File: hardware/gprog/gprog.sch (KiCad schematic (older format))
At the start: 23 parts, among them IC1 ATMEGA48P, P1 ISP x2560, P2 USB, P3 ISP x48, U1 74HC126, X1 12MHz

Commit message: gPROG: Dare I say the last, final draft.
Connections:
- net at U1.1, U1.13 (~E): now also JP1.2, R8.1, U1.10 (~E), U1.4 (~E)
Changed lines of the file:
@@
-EESchema Schematic File Version 2  date 27/11/2011 12:21:00 p.m.
+EESchema Schematic File Version 2  date 27/11/2011 8:31:10 p.m.
 LIBS:power
 LIBS:device
@@
 Sheet 1 1
 Title "G9X USB Programmer"
-Date "26 nov 2011"
+Date "27 nov 2011"
 Rev "1.0"
 Comp ""
@@
 Comment4 ""
 $EndDescr
+Connection ~ 7150 2400
+Wire Wire Line
+	8050 2400 7100 2400
+Connection ~ 8850 5150
+Wire Wire Line
+	8850 4750 8850 5150
+Wire Wire Line
+	6250 3200 6000 3200
+Wire Wire Line
+	6000 3200 6000 3450
+Wire Wire Line
+	7150 2400 7150 3950
+Wire Wire Line
+	7150 3950 8000 3950
+Wire Wire Line
+	8000 3950 8000 4000
+Connection ~ 1750 3550
+Wire Wire Line
+	1750 4350 1750 4100
+Wire Wire Line
+	1350 4100 1350 4250
+Wire Wire Line
+	1350 4250 2150 4250
+Wire Wire Line
+	2150 4250 2150 4100
+Connection ~ 2750 6950
+Wire Wire Line
+	2750 7050 2750 6950
+Connection ~ 3100 6350
+Wire Wire Line
+	3100 6500 3100 6350
+Wire Wire Line
+	2450 6350 2350 6350
+Wire Wire Line
+	3200 6350 3050 6350
+Connection ~ 2550 5850
+Wire Wire Line
+	2550 5750 2550 5850
+Wire Wire Line
+	3200 5150 2900 5150
+Wire Wire Line
+	3200 5350 2900 5350
+Wire Wire Line
+	3200 5550 2900 5550
+Wire Wire Line
+	5150 5550 5450 5550
+Connection ~ 4200 6850
+Wire Wire Line
+	4300 6850 4100 6850
+Wire Wire Line
+	4200 3950 4200 4100
+Wire Wire Line
+	9600 5550 9300 5550
+Wire Wire Line
+	9600 5350 9000 5350
+Wire Wire Line
+	9600 5150 8600 5150
+Wire Wire Line
+	7600 1950 6750 1950
+Wire Wire Line
+	7250 3600 6750 3600
+Wire Wire Line
+	9600 3150 9450 3150
+Wire Wire Line
+	9450 3150 9450 3550
+Wire Wire Line
+	9600 3050 8400 3050
+Wire Wire Line
+	8400 3050 8400 3600
+Wire Wire Line
+	8400 3600 8150 3600
+Connection ~ 8050 2400
+Wire Wire Line
+	9600 2650 9150 2650
+Wire Wire Line
+	9150 2650 9150 1950
+Wire Wire Line
+	9150 1950 8500 1950
+Wire Wire Line
+	2500 2600 2500 2250
+Wire Wire Line
+	2500 2600 2550 2600
+Wire Wire Line
+	4150 1950 4150 1700
+Wire Wire Line
+	5000 1800 5300 1800
+Wire Wire Line
+	3250 3150 3250 3050
+Connection ~ 3600 2600
+Wire Wire Line
+	3600 2650 3600 2600
+Wire Wire Line
+	3250 2600 3250 2650
+Wire Wire Line
+	3050 2600 4500 2600
+Wire Wire Line
+	3800 2350 3800 2400
+Connection ~ 4150 1800
+Wire Wire Line
+	2500 2250 1950 2250
+Wire Wire Line
+	2200 1800 2200 2050
+Wire Wire Line
+	2200 2050 1950 2050
+Wire Wire Line
+	1950 2350 2200 2350
+Wire Wire Line
+	2200 2350 2200 2650
+Wire Wire Line
+	2500 2150 2500 1800
+Wire Wire Line
+	2500 2150 1950 2150
+Wire Wire Line
+	3800 1950 3800 1800
+Connection ~ 3800 1800
+Wire Wire Line
+	4150 2400 4150 2350
+Connection ~ 3250 2600
+Wire Wire Line
+	3600 3050 3600 3150
+Wire Wire Line
+	5000 2600 5300 2600
+Wire Wire Line
+	4150 1200 4150 1150
+Wire Wire Line
+	4500 1800 3100 1800
+Wire Wire Line
+	2500 1800 2600 1800
+Wire Wire Line
+	9600 2850 8500 2850
+Wire Wire Line
+	9600 2750 8800 2750
+Wire Wire Line
+	8800 2750 8800 2400
+Wire Wire Line
+	8050 2250 8050 2550
+Wire Wire Line
+	8450 4300 8800 4300
+Wire Wire Line
+	8800 4300 8800 2950
+Wire Wire Line
+	8800 2950 9600 2950
+Wire Wire Line
+	7550 4300 6750 4300
+Wire Wire Line
+	7600 2850 6750 2850
+Wire Wire Line
+	9600 5050 9000 5050
+Wire Wire Line
+	9600 5250 9000 5250
+Wire Wire Line
+	9600 5450 9000 5450
+Wire Wire Line
+	9300 5550 9300 5800
+Wire Wire Line
+	4300 4100 4100 4100
+Connection ~ 4200 4100
+Wire Wire Line
+	4200 7000 4200 6850
+Wire Wire Line
+	3200 5650 2900 5650
+Wire Wire Line
+	3200 5450 2900 5450
+Wire Wire Line
+	3200 5250 2900 5250
+Wire Wire Line
+	2100 5850 3200 5850
+Wire Wire Line
+	2550 5150 2550 5250
+Wire Wire Line
+	3200 6150 2350 6150
+Wire Wire Line
+	2350 6150 2350 6500
+Connection ~ 2350 6350
+Wire Wire Line
+	3100 6900 3100 6950
+Wire Wire Line
+	3100 6950 2350 6950
+Wire Wire Line
+	2350 6950 2350 6900
+Wire Wire Line
+	6500 2150 6500 2400
+Wire Wire Line
+	6500 2400 6600 2400
+Connection ~ 1750 4250
+Wire Wire Line
+	1350 3700 1350 3550
+Wire Wire Line
+	1350 3550 2150 3550
+Wire Wire Line
+	2150 3550 2150 3700
+Wire Wire Line
+	1750 3450 1750 3700
+Wire Wire Line
+	7700 3300 7700 3200
+Connection ~ 7150 3200
+Wire Wire Line
+	7700 3200 6850 3200
+Wire Wire Line
+	8600 5150 8600 4750
 $Comp
 L +5V #PWR01
@@
 	1    0    0    -1
 $EndComp
-Wire Wire Line
-	8600 5150 8600 4750
-Wire Wire Line
-	6850 3200 7700 3200
-Connection ~ 7150 3200
-Wire Wire Line
-	7700 3200 7700 3300
-Wire Wire Line
-	1750 3450 1750 3700
-Wire Wire Line
-	2150 3550 2150 3700
-Wire Wire Line
-	2150 3550 1350 3550
-Wire Wire Line
-	1350 3550 1350 3700
-Connection ~ 1750 4250
-Wire Wire Line
-	6600 2400 6500 2400
-Wire Wire Line
-	6500 2400 6500 2150
-Wire Wire Line
-	2350 6950 2350 6900
-Wire Wire Line
-	2350 6950 3100 6950
-Wire Wire Line
-	3100 6950 3100 6900
-Connection ~ 2350 6350
-Wire Wire Line
-	2350 6500 2350 6150
-Wire Wire Line
-	2350 6150 3200 6150
-Wire Wire Line
-	2550 5150 2550 5250
-Wire Wire Line
-	2100 5850 3200 5850
-Wire Wire Line
-	3200 5250 2900 5250
-Wire Wire Line
-	3200 5450 2900 5450
-Wire Wire Line
-	3200 5650 2900 5650
-Wire Wire Line
-	4200 7000 4200 6850
-Connection ~ 4200 4100
-Wire Wire Line
-	4300 4100 4100 4100
-Wire Wire Line
-	9300 5800 9300 5550
-Wire Wire Line
-	9600 5450 9000 5450
-Wire Wire Line
-	9600 5250 9000 5250
-Wire Wire Line
-	9600 5050 9000 5050
-Wire Wire Line
-	7600 2850 6750 2850
-Wire Wire Line
-	7550 4300 6750 4300
-Wire Wire Line
-	9600 2950 8800 2950
-Wire Wire Line
-	8800 2950 8800 4300
-Wire Wire Line
-	8800 4300 8450 4300
-Wire Wire Line
-	8050 2250 8050 2550
-Wire Wire Line
-	8800 2400 8800 2750
-Wire Wire Line
-	8800 2750 9600 2750
-Wire Wire Line
-	9600 2850 8500 2850
-Wire Wire Line
-	2600 1800 2500 1800
-Wire Wire Line
-	4500 1800 3100 1800
-Wire Wire Line
-	4150 1200 4150 1150
-Wire Wire Line
-	5000 2600 5300 2600
-Wire Wire Line
-	3600 3050 3600 3150
-Connection ~ 3250 2600
-Wire Wire Line
-	4150 2400 4150 2350
-Connection ~ 3800 1800
-Wire Wire Line
-	3800 1950 3800 1800
-Wire Wire Line
-	1950 2150 2500 2150
-Wire Wire Line
-	2500 2150 2500 1800
-Wire Wire Line
-	2200 2650 2200 2350
-Wire Wire Line
-	2200 2350 1950 2350
-Wire Wire Line
-	1950 2050 2200 2050
-Wire Wire Line
-	2200 2050 2200 1800
-Wire Wire Line
-	1950 2250 2500 2250
-Connection ~ 4150 1800
-Wire Wire Line
-	3800 2350 3800 2400
-Wire Wire Line
-	3050 2600 4500 2600
-Wire Wire Line
-	3250 2600 3250 2650
-Wire Wire Line
-	3600 2650 3600 2600
-Connection ~ 3600 2600
-Wire Wire Line
-	3250 3150 3250 3050
-Wire Wire Line
-	5000 1800 5300 1800
-Wire Wire Line
-	4150 1950 4150 1700
-Wire Wire Line
-	2550 2600 2500 2600
-Wire Wire Line
-	2500 2600 2500 2250
-Wire Wire Line
-	8500 1950 9150 1950
-Wire Wire Line
-	9150 1950 9150 2650
-Wire Wire Line
-	9150 2650 9600 2650
-Connection ~ 8050 2400
-Wire Wire Line
-	8150 3600 8400 3600
-Wire Wire Line
-	8400 3600 8400 3050
-Wire Wire Line
-	8400 3050 9600 3050
-Wire Wire Line
-	9450 3550 9450 3150
-Wire Wire Line
-	9450 3150 9600 3150
-Wire Wire Line
-	7250 3600 6750 3600
-Wire Wire Line
-	7600 1950 6750 1950
-Wire Wire Line
-	9600 5150 8600 5150
-Wire Wire Line
-	9600 5350 9000 5350
-Wire Wire Line
-	9300 5550 9600 5550
-Wire Wire Line
-	4200 3950 4200 4100
-Wire Wire Line
-	4300 6850 4100 6850
-Connection ~ 4200 6850
-Wire Wire Line
-	5150 5550 5450 5550
-Wire Wire Line
-	3200 5550 2900 5550
-Wire Wire Line
-	3200 5350 2900 5350
-Wire Wire Line
-	3200 5150 2900 5150
-Wire Wire Line
-	2550 5750 2550 5850
-Connection ~ 2550 5850
-Wire Wire Line
-	3200 6350 3050 6350
-Wire Wire Line
-	2450 6350 2350 6350
-Wire Wire Line
-	3100 6500 3100 6350
-Connection ~ 3100 6350
-Wire Wire Line
-	2750 7050 2750 6950
-Connection ~ 2750 6950
-Wire Wire Line
-	2150 4250 2150 4100
-Wire Wire Line
-	2150 4250 1350 4250
-Wire Wire Line
-	1350 4250 1350 4100
-Wire Wire Line
-	1750 4350 1750 4100
-Connection ~ 1750 3550
-Wire Wire Line
-	8000 4000 8000 3950
-Wire Wire Line
-	7150 3950 8000 3950
-Wire Wire Line
-	7150 2400 7150 3950
-Connection ~ 7150 2400
-Wire Wire Line
-	6000 3450 6000 3200
-Wire Wire Line
-	6000 3200 6250 3200
-Wire Wire Line
-	8850 4750 8850 5150
-Connection ~ 8850 5150
 $Comp
 L VCC #PWR02

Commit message: Major changes to gprog, after prototype revealed multiple problems. Also reverted to TQFP-32 package instead of QFN/MLF.
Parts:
- removed JP1: ENABLE, symbol JUMPER
- added D5, D6: LED, symbol LED
- added D7: DIODESCH, symbol DIODESCH
- added R4, R9: 1K, symbol R
- U1: value 74HC126 -> 74HC125; symbol 74LS126 -> 74LS125
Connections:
- net labels added: BUF_ENABLE
- wire segments 92 -> 101
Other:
- note added: "Target Vcc is \n74HC125 only"
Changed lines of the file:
@@
-EESchema Schematic File Version 2  date 27/11/2011 8:31:10 p.m.
+EESchema Schematic File Version 2  date 13/12/2011 4:09:18 p.m.
 LIBS:power
 LIBS:device
@@
 Sheet 1 1
 Title "G9X USB Programmer"
-Date "27 nov 2011"
-Rev "1.0"
+Date "13 dec 2011"
+Rev "0.2"
 Comp ""
 Comment1 "Customised for G9X by JWB. Converted ro KiCAD by Gruvin"
@@
 Comment4 ""
 $EndDescr
+$Comp
+L VCC #PWR?
+U 1 1 4EE6C1C8
+P 8800 2400
+F 0 "#PWR?" H 8800 2500 30  0001 C CNN
+F 1 "VCC" H 8800 2500 30  0000 C CNN
+	1    8800 2400
+	1    0    0    -1
+$EndComp
+Text Notes 7300 5350 0    60   ~ 0
+Target Vcc is \n74HC125 only
+Wire Wire Line
+	8000 5150 7750 5150
+Connection ~ 5500 3150
+Wire Wire Line
+	5500 3050 5500 3150
+Wire Wire Line
+	5700 3750 5700 3850
+Wire Wire Line
+	5700 4250 5700 4650
+Wire Wire Line
+	5700 4650 5150 4650
+Wire Wire Line
+	5150 4850 5800 4850
 Connection ~ 7150 2400
 Wire Wire Line
-	8050 2400 7100 2400
-Connection ~ 8850 5150
-Wire Wire Line
-	8850 4750 8850 5150
-Wire Wire Line
-	6250 3200 6000 3200
-Wire Wire Line
-	6000 3200 6000 3450
+	7100 2400 8050 2400
 Wire Wire Line
 	7150 2400 7150 3950
@@
 	9600 5350 9000 5350
 Wire Wire Line
-	9600 5150 8600 5150
-Wire Wire Line
 	7600 1950 6750 1950
 Wire Wire Line
@@
 Connection ~ 3600 2600
 Wire Wire Line
-	3600 2650 3600 2600
-Wire Wire Line
-	3250 2600 3250 2650
+	3600 2600 3600 2650
+Wire Wire Line
+	3250 2650 3250 2600
 Wire Wire Line
 	3050 2600 4500 2600
@@
 	2500 2150 1950 2150
 Wire Wire Line
-	3800 1950 3800 1800
+	3800 1800 3800 1950
 Connection ~ 3800 1800
 Wire Wire Line
@@
 Connection ~ 7150 3200
 Wire Wire Line
-	7700 3200 6850 3200
+	7700 3200 6450 3200
 Wire Wire Line
 	8600 5150 8600 4750
+Wire Wire Line
+	5150 4550 5300 4550
+Wire Wire Line
+	5300 4550 5300 4250
+Wire Wire Line
+	5300 3850 5300 3750
+Wire Wire Line
+	5300 3250 5300 3150
+Wire Wire Line
+	5300 3150 5700 3150
+Wire Wire Line
+	5700 3150 5700 3250
+Wire Wire Line
+	8400 5150 9600 5150
+Connection ~ 8600 5150
+$Comp
+L DIODESCH D7
+U 1 1 4EE6C02E
+P 8200 5150
+F 0 "D7" H 8200 5250 40  0000 C CNN
+F 1 "DIODESCH" H 8200 5050 40  0000 C CNN
+	1    8200 5150
+	-1   0    0    1
+$EndComp
 $Comp
 L +5V #PWR01
-U 1 1 4ED164AA
-P 8800 2400
-F 0 "#PWR01" H 8800 2490 20  0001 C CNN
-F 1 "+5V" H 8800 2490 30  0000 C CNN
-	1    8800 2400
-	1    0    0    -1
-$EndComp
-$Comp
-L VCC #PWR02
+U 1 1 4EE6B3E0
+P 5500 3050
+F 0 "#PWR01" H 5500 3140 20  0001 C CNN
+F 1 "+5V" H 5500 3140 30  0000 C CNN
+	1    5500 3050
+	1    0    0    -1
+$EndComp
+$Comp
+L R R9
+U 1 1 4EE6B3BF
+P 5700 3500
+F 0 "R9" V 5780 3500 50  0000 C CNN
+F 1 "1K" V 5700 3500 50  0000 C CNN
+	1    5700 3500
+	-1   0    0    1
+$EndComp
+$Comp
+L R R4
+U 1 1 4EE6B3B8
+P 5300 3500
+F 0 "R4" V 5380 3500 50  0000 C CNN
+F 1 "1K" V 5300 3500 50  0000 C CNN
+	1    5300 3500
+	-1   0    0    1
+$EndComp
+$Comp
+L LED D6
+U 1 1 4EE6B3A6
+P 5700 4050
+F 0 "D6" H 5700 4150 50  0000 C CNN
+F 1 "LED" H 5700 3950 50  0000 C CNN
+	1    5700 4050
+	0    1    1    0
+$EndComp
+$Comp
+L LED D5
+U 1 1 4EE6B39B
+P 5300 4050
+F 0 "D5" H 5300 4150 50  0000 C CNN
+F 1 "LED" H 5300 3950 50  0000 C CNN
+	1    5300 4050
+	0    1    1    0
+$EndComp
+Text Label 6450 3200 0    60   ~ 0
+BUF_ENABLE
+Text Label 5250 4850 0    60   ~ 0
+BUF_ENABLE
+$Comp
+L VCC #PWR03
 U 1 1 4ED0B44E
-P 8850 4750
-F 0 "#PWR02" H 8850 4850 30  0001 C CNN
-F 1 "VCC" H 8850 4850 30  0000 C CNN
-	1    8850 4750
-	1    0    0    -1
-$EndComp
-$Comp
-L GND #PWR03
-U 1 1 4ED0AC2D
-P 6000 3450
-F 0 "#PWR03" H 6000 3450 30  0001 C CNN
-F 1 "GND" H 6000 3380 30  0001 C CNN
-	1    6000 3450
-	1    0    0    -1
-$EndComp
-$Comp
-L JUMPER JP1
-U 1 1 4ED0AC1E
-P 6550 3200
-F 0 "JP1" H 6550 3350 60  0000 C CNN
-F 1 "ENABLE" H 6550 3120 40  0000 C CNN
-	1    6550 3200
-	1    0    0    -1
+P 7750 5150
+F 0 "#PWR03" H 7750 5250 30  0001 C CNN
+F 1 "VCC" H 7750 5250 30  0000 C CNN
+	1    7750 5150
+	0    -1   -1   0
 $EndComp
 $Comp
@@
 $EndComp
 $Comp
-L 74LS126 U1
+L 74LS125 U1
 U 2 1 4ECB2B38
 P 7700 3600
 F 0 "U1" H 7800 3800 60  0000 C CNN
-F 1 "74HC126" H 7950 3450 60  0000 C CNN
+F 1 "74HC125" H 7950 3450 60  0000 C CNN
 	2    7700 3600
 	1    0    0    1
 $EndComp
 $Comp
-L 74LS126 U1
+L 74LS125 U1
 U 3 1 4ECB2B37
 P 8000 4300
 F 0 "U1" H 8100 4500 60  0000 C CNN
-F 1 "74HC126" H 8250 4150 60  0000 C CNN
+F 1 "74HC125" H 8250 4150 60  0000 C CNN
 	3    8000 4300
 	1    0    0    1
 $EndComp
 $Comp
-L 74LS126 U1
+L 74LS125 U1
 U 1 1 4ECB2B35
 P 8050 2850
 F 0 "U1" H 8150 3050 60  0000 C CNN
-F 1 "74HC126" H 8300 2700 60  0000 C CNN
+F 1 "74HC125" H 8300 2700 60  0000 C CNN
 	1    8050 2850
 	1    0    0    1
 $EndComp
 $Comp
-L 74LS126 U1
+L 74LS125 U1
 U 4 1 4ECB2AFA
 P 8050 1950
 F 0 "U1" H 8150 2150 60  0000 C CNN
-F 1 "74HC126" H 8300 1800 60  0000 C CNN
+F 1 "74HC125" H 8300 1800 60  0000 C CNN
 	4    8050 1950
 	-1   0    0    -1

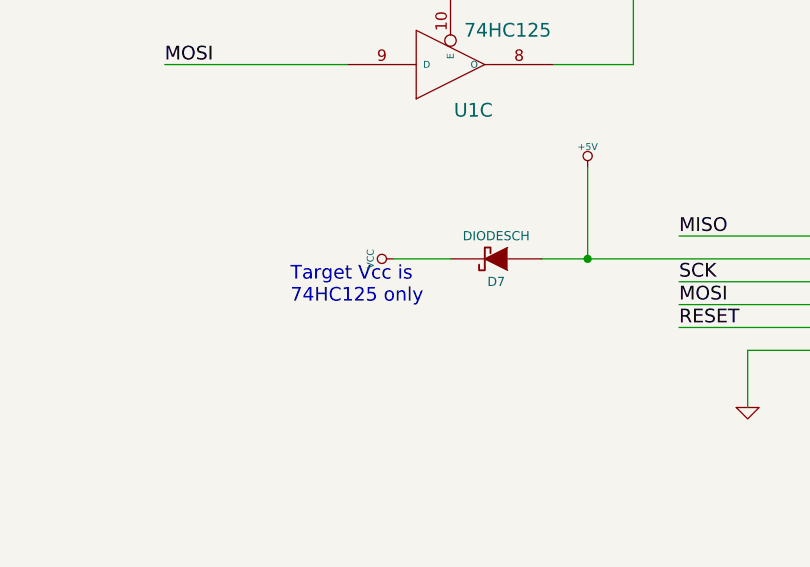
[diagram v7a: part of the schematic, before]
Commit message: GPROG: "Final" tinkerings. This version awaits comment by Jim before possibly ordering first KiCAD based prototype boards.
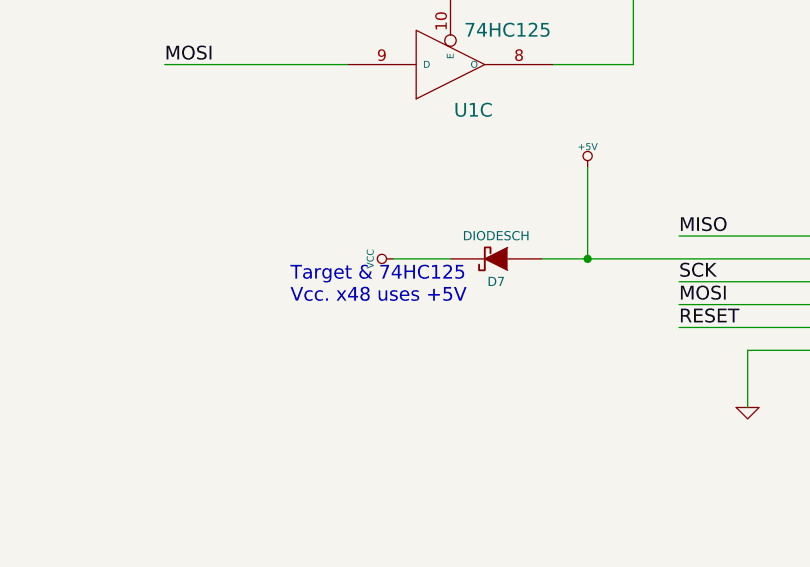
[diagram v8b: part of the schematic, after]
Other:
- note added: "Target & 74HC125 \nVcc. x48 uses +5V"
- note removed: "Target Vcc is \n74HC125 only"
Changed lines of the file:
@@
-EESchema Schematic File Version 2  date 13/12/2011 4:09:18 p.m.
+EESchema Schematic File Version 2  date 13/12/2011 6:23:52 p.m.
 LIBS:power
 LIBS:device
@@
 $EndDescr
 $Comp
-L VCC #PWR?
+L VCC #PWR01
 U 1 1 4EE6C1C8
 P 8800 2400
-F 0 "#PWR?" H 8800 2500 30  0001 C CNN
+F 0 "#PWR01" H 8800 2500 30  0001 C CNN
 F 1 "VCC" H 8800 2500 30  0000 C CNN
 	1    8800 2400
@@
 $EndComp
 Text Notes 7300 5350 0    60   ~ 0
-Target Vcc is \n74HC125 only
+Target & 74HC125 \nVcc. x48 uses +5V
 Wire Wire Line
 	8000 5150 7750 5150
@@
 $EndComp
 $Comp
-L +5V #PWR01
+L +5V #PWR02
 U 1 1 4EE6B3E0
 P 5500 3050
-F 0 "#PWR01" H 5500 3140 20  0001 C CNN
+F 0 "#PWR02" H 5500 3140 20  0001 C CNN
 F 1 "+5V" H 5500 3140 30  0000 C CNN
 	1    5500 3050
